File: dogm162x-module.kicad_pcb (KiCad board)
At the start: 2 copper layers, 62 x 33 mm, 6 parts, among them P1 CONN_01X08

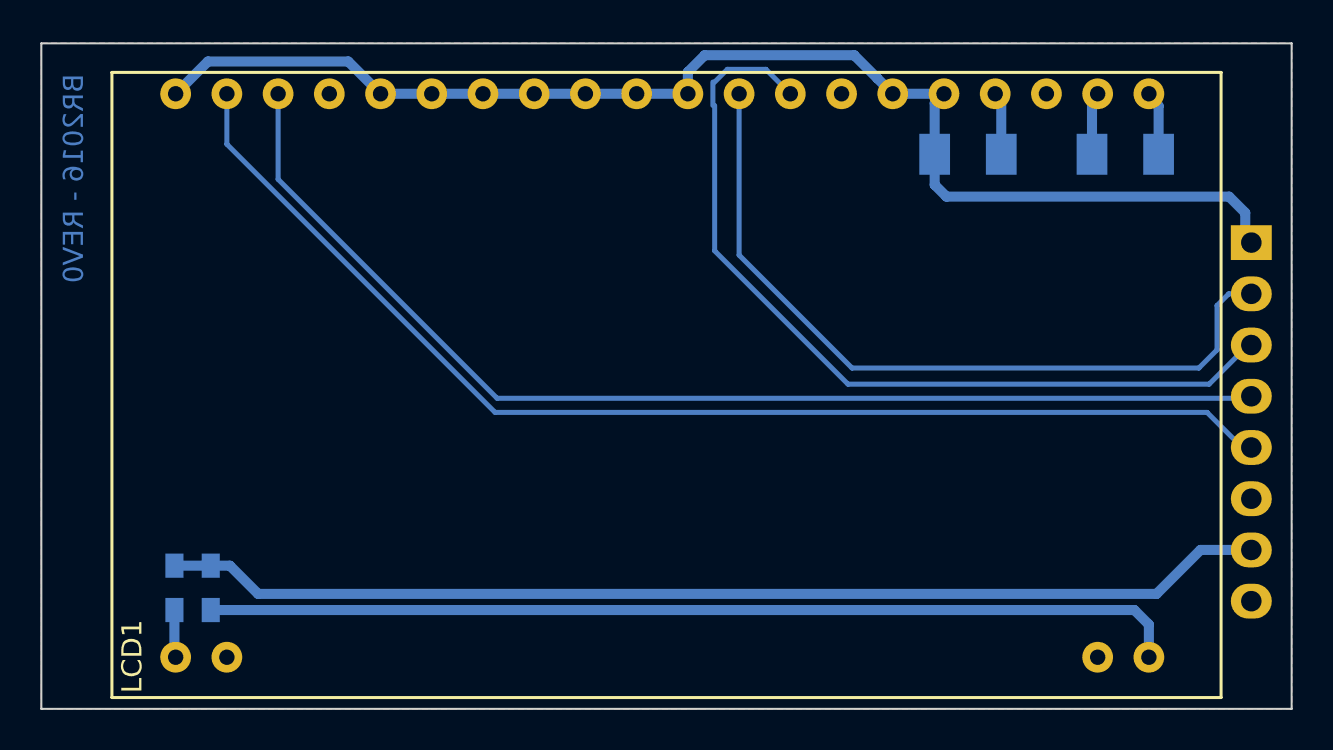
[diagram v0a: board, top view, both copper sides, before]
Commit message: added serial connection of LEDs and fixed 3d model path in parts
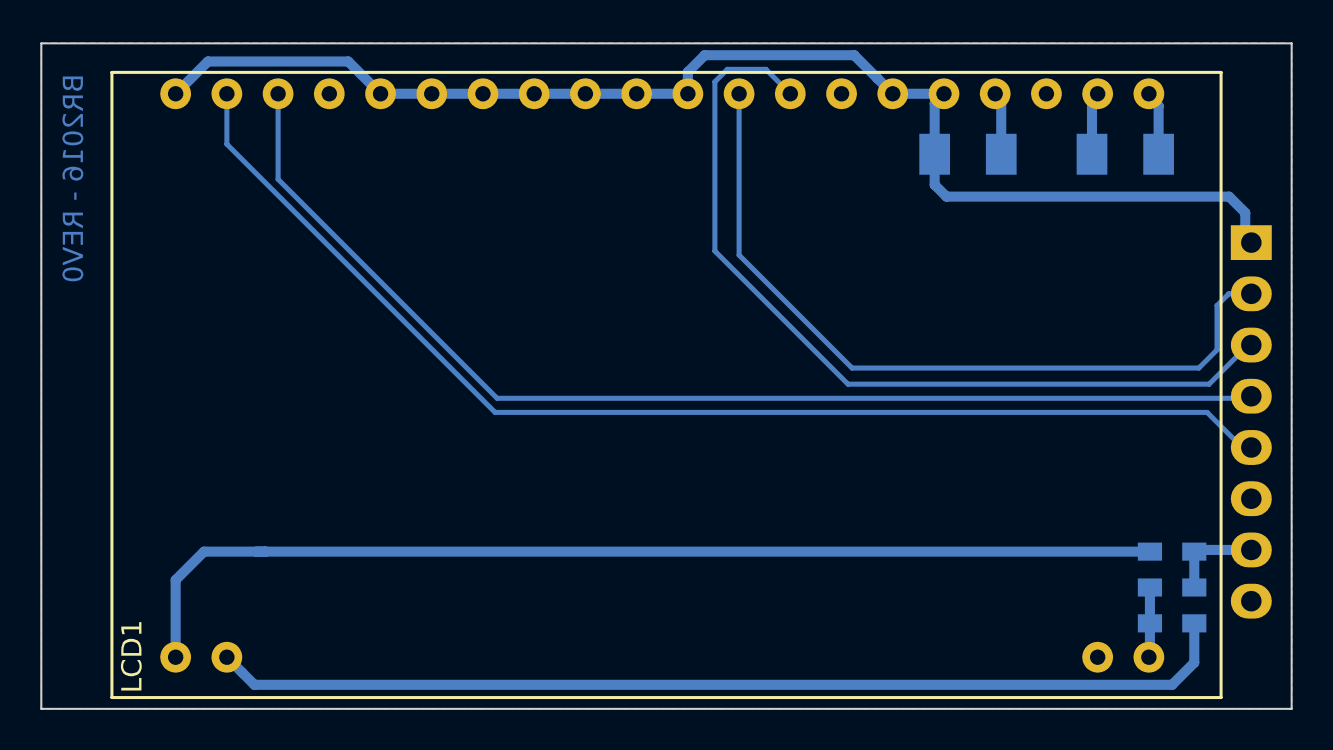
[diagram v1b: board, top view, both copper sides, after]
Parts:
- added R3: 0R, Resistors_SMD:R_0603_HandSoldering, B.Cu at (195.1, 111.8)
- moved R1 49.5 mm to (195.1, 108.2), turned to 180 degrees
- moved R2 47.7 mm to (195.1, 110.0), turned to 180 degrees
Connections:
- LCD1 pad 2: GND -> /C1
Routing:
- net /C1: track 0.00 -> 50.9 mm
- net /A1: track 2.36 -> 53.3 mm
- net /VCC_BACKLIGHT: track 54.6 -> 4.64 mm
- net /A2: track 48.5 -> 3.56 mm

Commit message: increased revision number and fixed circuit at C1
- increased revision number to Rev1 on schematic and pcb
- an additional resistor is necessary to connect C1 to GND
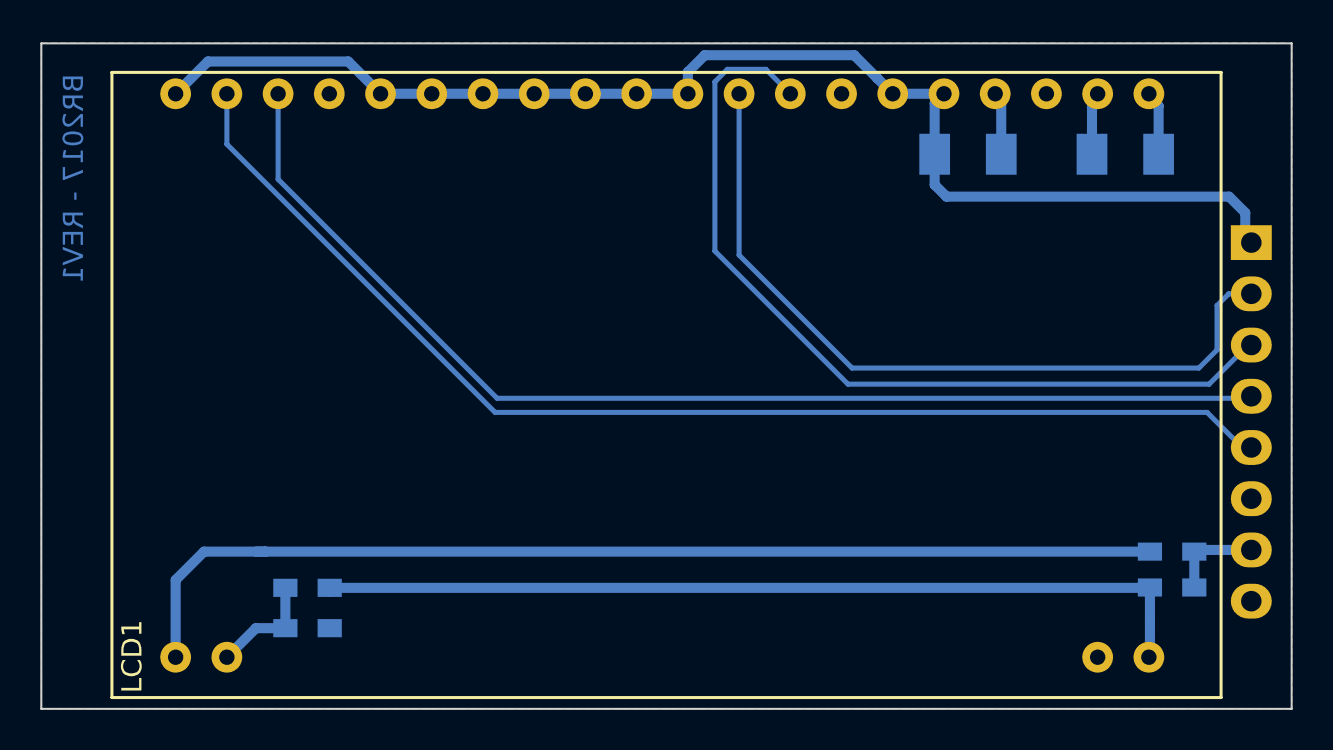
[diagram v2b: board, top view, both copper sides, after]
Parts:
- added R4: 0R, Resistors_SMD:R_0603_HandSoldering, B.Cu at (152.2, 112.0)
- moved R3 42.9 mm to (152.2, 110.0), turned to 180 degrees
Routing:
- net /C1: track 50.9 -> 5.30 mm
- net /A2: track 3.56 -> 44.3 mm
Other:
- board text added: "BR2017 - REV1"
- board text removed: "BR2016 - REV0"
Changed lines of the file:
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@@
 (kicad_pcb (version 4) (host pcbnew 4.0.4-1.fc25-product)
   (general
-    (links 29)
+    (links 31)
     (no_connects 0)
     (area 138.949999 82.949999 201.050001 116.050001)
     (thickness 1.6)
     (drawings 19)
-    (tracks 74)
+    (tracks 75)
     (zones 0)
-    (modules 7)
+    (modules 8)
     (nets 14)
   )
@@
   )
   (setup
-    (last_trace_width 0.25)
+    (last_trace_width 0.5)
     (user_trace_width 0.5)
     (trace_clearance 0.2)
@@
     (add_net VCC)
   )
+  (module Resistors_SMD:R_0603_HandSoldering (layer B.Cu)
+    (at 152.2 112 180)
+    (descr "Resistor SMD 0603, hand soldering")
+    (tags "resistor 0603")
+    (attr smd)
+    (fp_text reference R4 (at -3 0 180) (layer B.SilkS)
+      (effects (font (size 1 1) (thickness 0.15)) (justify mirror))
+    )
+    (fp_text value 0R (at 0 -1.9 180) (layer B.Fab)
+      (effects (font (size 1 1) (thickness 0.15)) (justify mirror))
+    )
+    (fp_line (start -0.8 -0.4) (end -0.8 0.4) (layer B.Fab) (width 0.1))
+    (fp_line (start 0.8 -0.4) (end -0.8 -0.4) (layer B.Fab) (width 0.1))
+    (fp_line (start 0.8 0.4) (end 0.8 -0.4) (layer B.Fab) (width 0.1))
+    (fp_line (start -0.8 0.4) (end 0.8 0.4) (layer B.Fab) (width 0.1))
+    (fp_line (start -2 0.8) (end 2 0.8) (layer B.CrtYd) (width 0.05))
+    (fp_line (start -2 -0.8) (end 2 -0.8) (layer B.CrtYd) (width 0.05))
+    (fp_line (start -2 0.8) (end -2 -0.8) (layer B.CrtYd) (width 0.05))
+    (fp_line (start 2 0.8) (end 2 -0.8) (layer B.CrtYd) (width 0.05))
+    (fp_line (start 0.5 -0.675) (end -0.5 -0.675) (layer B.SilkS) (width 0.15))
+    (fp_line (start -0.5 0.675) (end 0.5 0.675) (layer B.SilkS) (width 0.15))
+    (pad 1 smd rect (at -1.1 0 180) (size 1.2 0.9) (layers B.Cu B.Paste B.Mask)
+      (net 6 GND))
+    (pad 2 smd rect (at 1.1 0 180) (size 1.2 0.9) (layers B.Cu B.Paste B.Mask)
+      (net 13 /C1))
+    (model Resistors_SMD.3dshapes/R_0603_HandSoldering.wrl
+      (at (xyz 0 0 0))
+      (scale (xyz 1 1 1))
+      (rotate (xyz 0 0 0))
+    )
+  )
   (module dogm162x:DOGM162X locked (layer F.Cu)
     (at 170 99.94)
@@
   )
   (module Resistors_SMD:R_0603_HandSoldering (layer B.Cu)
-    (at 195.072 111.76)
+    (at 152.2 110 180)
     (descr "Resistor SMD 0603, hand soldering")
     (tags "resistor 0603")
     (attr smd)
-    (fp_text reference R3 (at -3.048 0 180) (layer B.SilkS)
-      (effects (font (size 1 1) (thickness 0.15)) (justify mirror))
-    )
-    (fp_text value 0R (at 0 -1.9) (layer B.Fab)
+    (fp_text reference R3 (at -3.048 0 360) (layer B.SilkS)
+      (effects (font (size 1 1) (thickness 0.15)) (justify mirror))
+    )
+    (fp_text value 0R (at 0 -1.9 180) (layer B.Fab)
       (effects (font (size 1 1) (thickness 0.15)) (justify mirror))
     )
@@
     (fp_line (start 0.5 -0.675) (end -0.5 -0.675) (layer B.SilkS) (width 0.15))
     (fp_line (start -0.5 0.675) (end 0.5 0.675) (layer B.SilkS) (width 0.15))
-    (pad 1 smd rect (at -1.1 0) (size 1.2 0.9) (layers B.Cu B.Paste B.Mask)
+    (pad 1 smd rect (at -1.1 0 180) (size 1.2 0.9) (layers B.Cu B.Paste B.Mask)
       (net 7 /A2))
-    (pad 2 smd rect (at 1.1 0) (size 1.2 0.9) (layers B.Cu B.Paste B.Mask)
+    (pad 2 smd rect (at 1.1 0 180) (size 1.2 0.9) (layers B.Cu B.Paste B.Mask)
       (net 13 /C1))
     (model ${KISYS3DMOD}/Resistors_SMD.3dshapes/R_0603.wrl
@@
     (effects (font (size 2 2) (thickness 0.3)) (justify mirror))
   )
-  (gr_text "BR2016 - REV0" (at 140.6 89.7 90) (layer B.Cu)
+  (gr_text "BR2017 - REV1" (at 140.6 89.7 90) (layer B.Cu)
     (effects (font (size 1 1) (thickness 0.15)) (justify mirror))
   )
@@
   (segment (start 147.066 108.204) (end 150.114 108.204) (width 0.5) (layer B.Cu) (net 5))
   (segment (start 145.6 113.38) (end 145.66 113.44) (width 0.5) (layer B.Cu) (net 5))
+  (segment (start 153.3 110.2) (end 153.5 110) (width 0.5) (layer B.Cu) (net 7))
+  (segment (start 153.5 110) (end 193.954 110) (width 0.5) (layer B.Cu) (net 7))
+  (segment (start 193.954 110) (end 193.972 109.982) (width 0.5) (layer B.Cu) (net 7))
   (segment (start 193.972 111.76) (end 193.972 113.388) (width 0.5) (layer B.Cu) (net 7))
   (segment (start 193.972 113.388) (end 193.92 113.44) (width 0.5) (layer B.Cu) (net 7))
@@
   (segment (start 199 108.12) (end 196.256 108.12) (width 0.5) (layer B.Cu) (net 12))
   (segment (start 196.256 108.12) (end 196.172 108.204) (width 0.5) (layer B.Cu) (net 12))
-  (segment (start 196.172 111.76) (end 196.172 113.708) (width 0.5) (layer B.Cu) (net 13))
-  (segment (start 196.172 113.708) (end 195.072 114.808) (width 0.5) (layer B.Cu) (net 13))
-  (segment (start 195.072 114.808) (end 149.568 114.808) (width 0.5) (layer B.Cu) (net 13))
-  (segment (start 149.568 114.808) (end 148.961999 114.201999) (width 0.5) (layer B.Cu) (net 13))
-  (segment (start 148.961999 114.201999) (end 148.2 113.44) (width 0.5) (layer B.Cu) (net 13))
+  (segment (start 151.1 112) (end 149.64 112) (width 0.5) (layer B.Cu) (net 13))
+  (segment (start 149.64 112) (end 148.2 113.44) (width 0.5) (layer B.Cu) (net 13))
+  (segment (start 151.1 110.2) (end 151.1 112) (width 0.5) (layer B.Cu) (net 13))
   (zone (net 6) (net_name GND) (layer B.Cu) (hatch edge 0.508)
     (connect_pads (clearance 0.508))

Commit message: added pin descriptions
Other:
- board text added: "VCC CLK SI CS RS GND"
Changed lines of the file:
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@@
     (area 138.949999 82.949999 201.050001 116.050001)
     (thickness 1.6)
-    (drawings 19)
+    (drawings 20)
     (tracks 75)
     (zones 0)
@@
   )
   (setup
-    (last_trace_width 0.5)
+    (last_trace_width 0.25)
     (user_trace_width 0.5)
     (trace_clearance 0.2)
@@
     )
   )
+  (gr_text "VCC\nCLK\nSI\nCS\nRS\nGND" (at 196.85 99.4) (layer B.SilkS)
+    (effects (font (size 1.5 1.5) (thickness 0.3)) (justify left mirror))
+  )
   (gr_text "DOG-M162X\nDisplay Module" (at 170 110) (layer B.SilkS)
